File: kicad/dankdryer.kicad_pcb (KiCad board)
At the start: 2 copper layers, 100 x 75 mm, 52 parts, among them J10 HeaderX4, J13 barreljack, J2 to microboard, J3 to baseboard, J4 ScrewX2, J5 ScrewX4, J6 LCD, J7 HeaderX4, J8 ScrewX2, J9 UART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

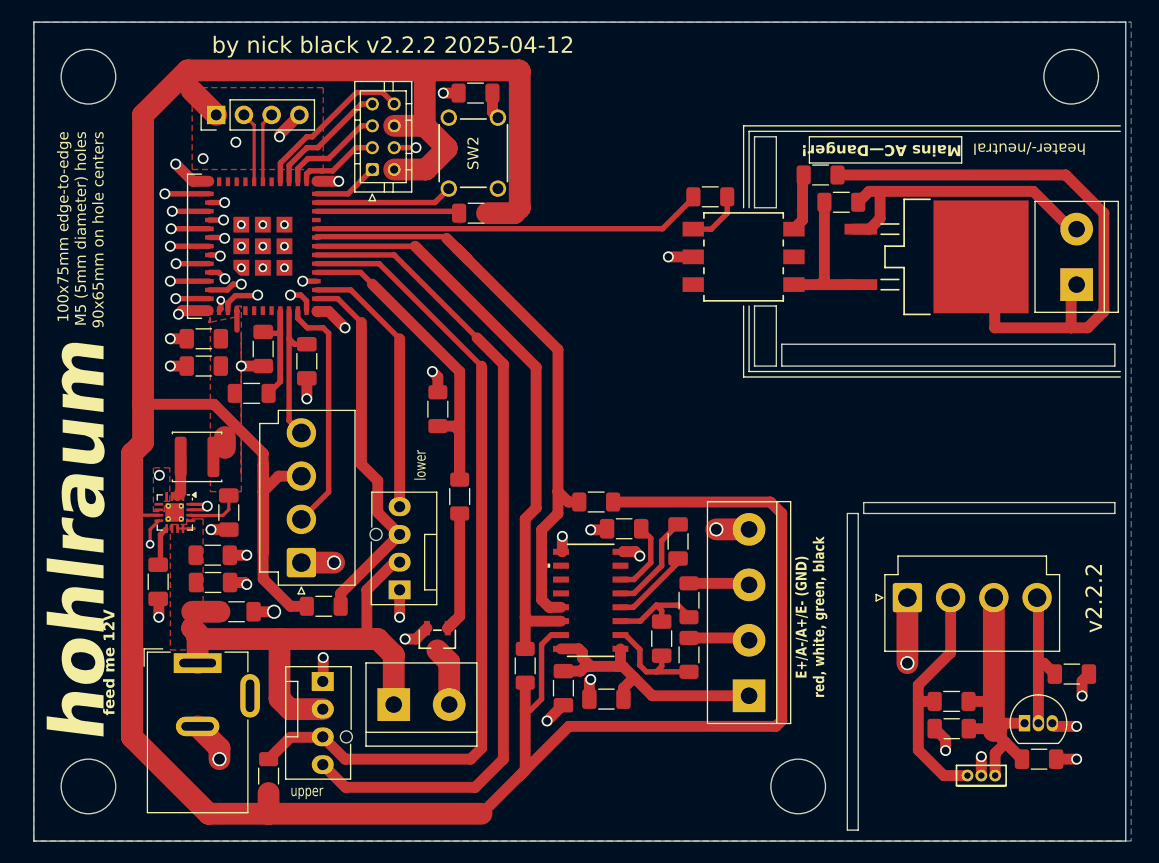
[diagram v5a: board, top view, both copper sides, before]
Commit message: [kicad] move to spring clips for load cell
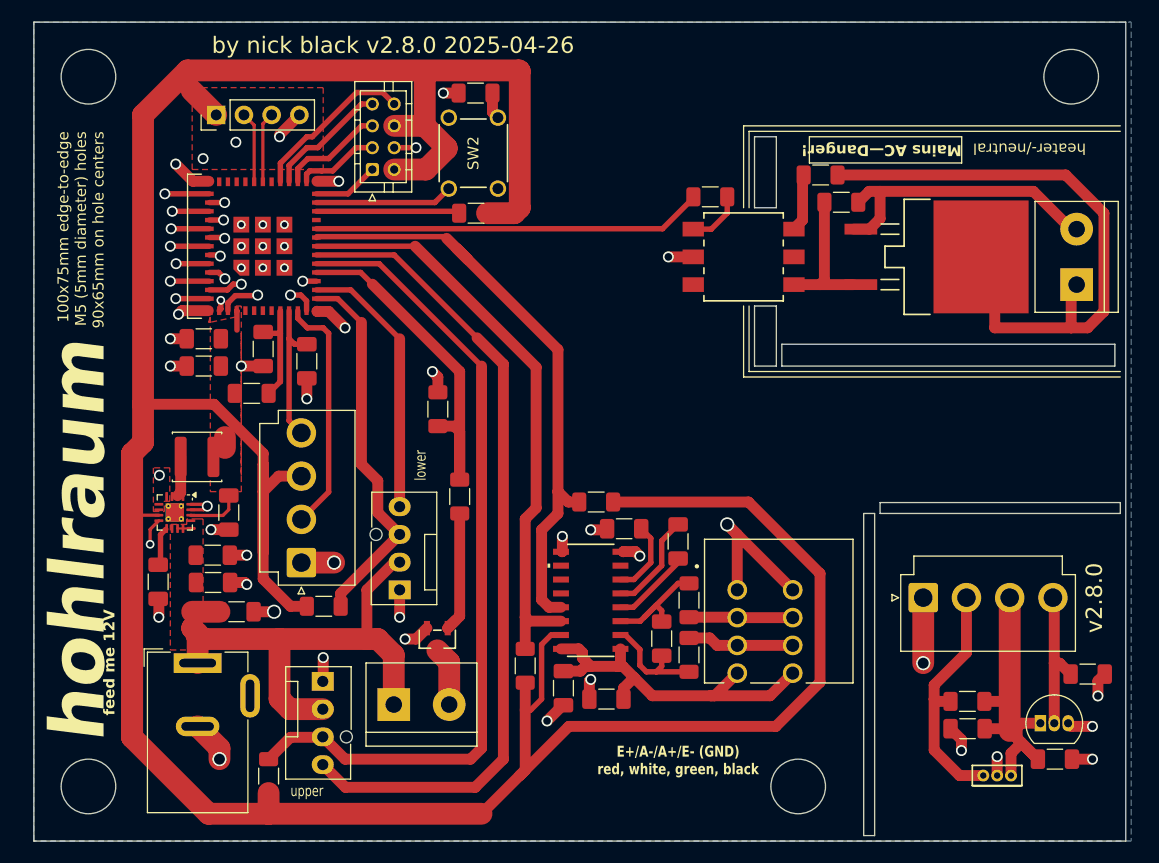
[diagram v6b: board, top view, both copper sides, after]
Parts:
- removed J5: ScrewX4, TerminalBlock:TerminalBlock_bornier-4_P5.08mm
- added J1: 1-2834016-4, dank:TE_1-2834016-4, F.Cu at (118.2, 103.9)
- moved Q1 1.45 mm to (139.5, 119.0)
- moved U5 1.45 mm to (142.2, 114.2)
- moved C17 1.45 mm to (146.5, 109.7)
- moved C19 1.45 mm to (143.5, 117.5)
- moved C4 1.45 mm to (135.5, 114.7)
- moved J3 1.45 mm to (131.4, 102.7)
- moved R20 1.45 mm to (135.5, 112.2)
- turned R11 to 90 degrees
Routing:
- net GND: track 128.0 -> 139.8 mm
- net E+: track 26.0 -> 34.2 mm
- net A-: track 5.28 -> 9.78 mm
- net A+: track 5.36 -> 9.46 mm
- net Net-(U3-VIN1P): track 9.00 -> 10.9 mm
- net +3.3V: track 327.2 -> 328.9 mm
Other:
- outline, holes or cut-outs redrawn

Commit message: [pcb] fatten a few traces
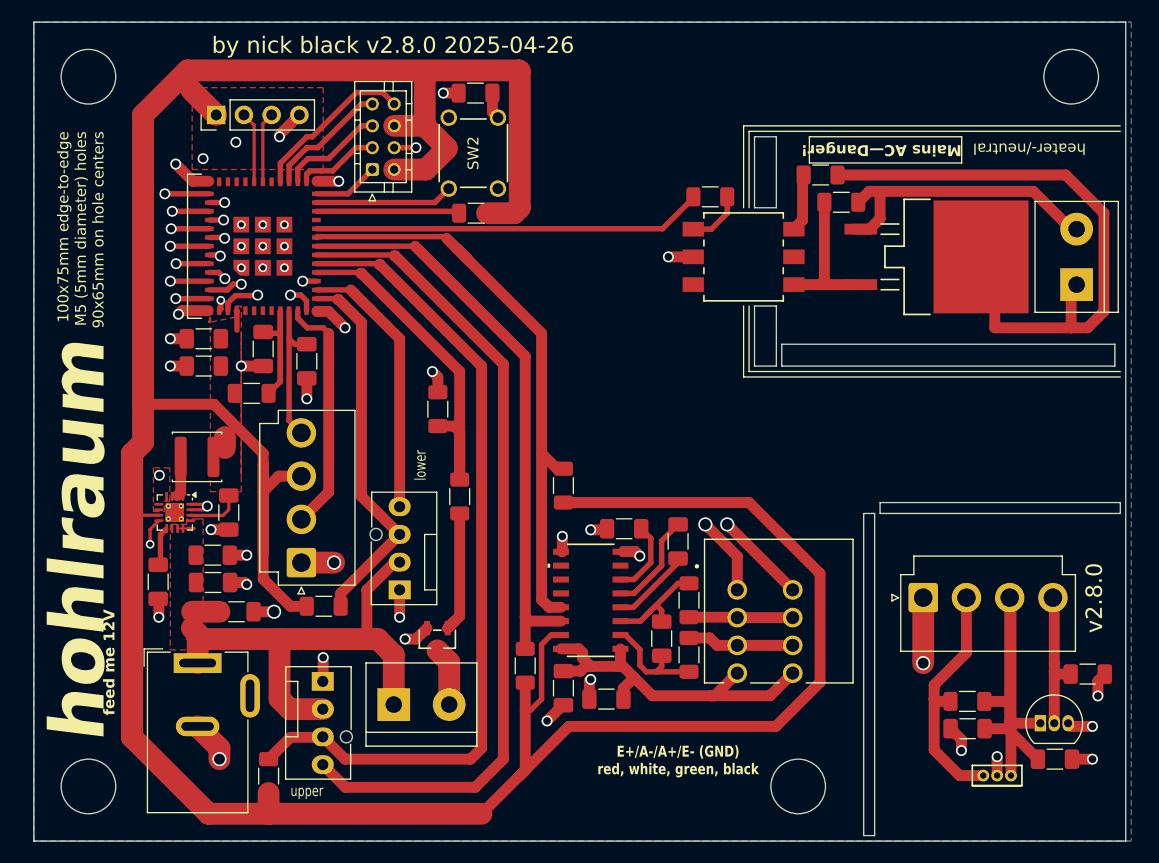
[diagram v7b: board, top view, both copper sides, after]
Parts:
- moved R6 3.35 mm to (98.5, 92.5), turned to 90 degrees
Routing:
- net +3.3Vmicro: track 28.9 -> 40.1 mm
- net +3.3V: track 328.9 -> 333.4 mm
- net /SCL: track 58.5 -> 57.5 mm
- net GND: track 139.8 -> 140.6 mm, vias 66 -> 67
- net /SDA: track 54.3 -> 53.5 mm
